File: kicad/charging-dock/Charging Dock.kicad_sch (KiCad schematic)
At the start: 0 parts

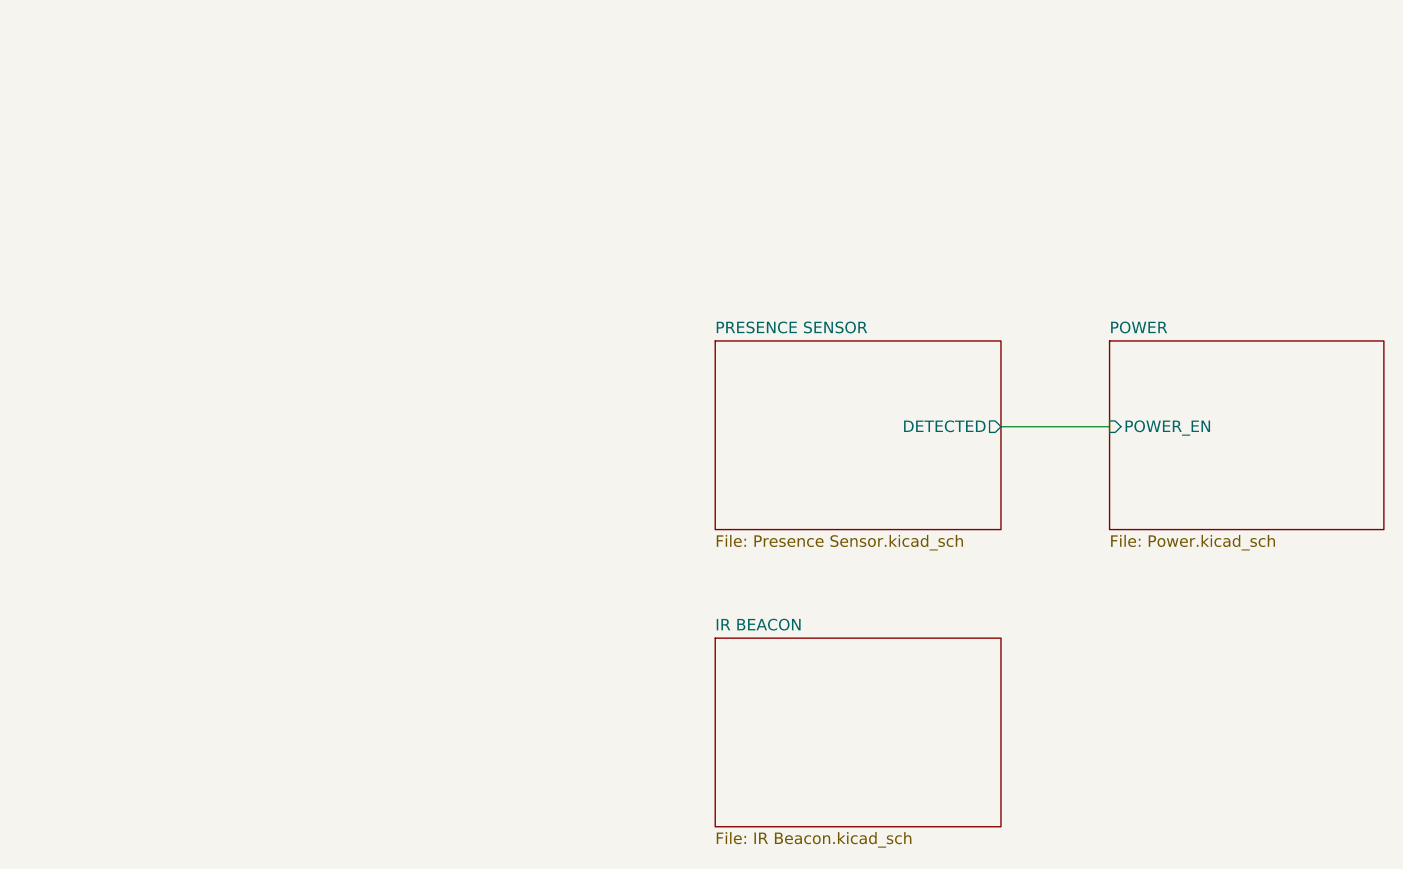
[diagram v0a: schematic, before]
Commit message: Charging dock rev 2; main-phone bucks AP64501 -> TPS54560B
Charging dock (kicad/charging-dock), redesigned:
- CH32V003F4P6 control (Arduino core, ch32fun, PlatformIO)
- robot detection: resistance-signature probe before DOCK+ goes live
- AO4407C soft-start output switch, 50 mOhm + INA180A1 current sense
- NEC IR beacon: two 3x TSAL6200 strings, AC-coupled gates
- 20 V input: DC-044A-20A, 5 A fuse, SMAJ22A, HT7533-1
- refs 8xxx for the one-panel plan; uses the shared ../main libraries
- removed the orphan sheets, the old local library copy and an unrelated PDF
- README with pin map, detection math, firmware rules, layout notes

main-phone: U21/U22 TPS54560B (AP64501 out of stock) with SS56 catch
diodes, 232k RT, 4.7k + 47nF compensation, U21 EN divider; BAT-VCC input
caps 10uF/50V 1206. SPEC and READMEs updated.

Co-Authored-By: Claude Opus 5.5 (1M context) <noreply@anthropic.com>
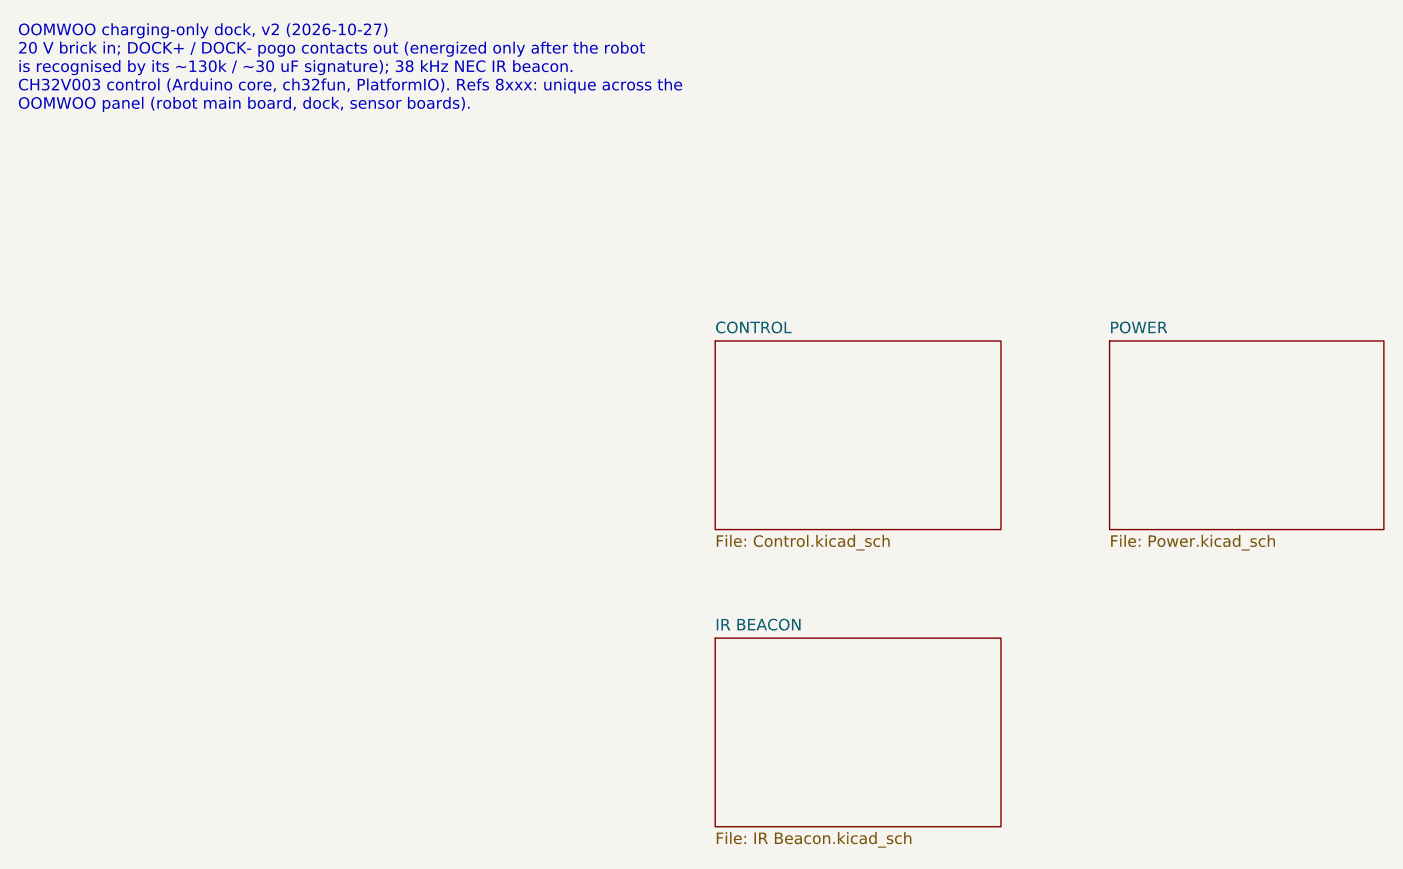
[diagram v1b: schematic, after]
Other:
- sheet PRESENCE SENSOR renamed CONTROL
- sheet CONTROL: file Presence Sensor.kicad_sch -> Control.kicad_sch
- sheet CONTROL ports: added none; removed DETECTED
- sheet POWER ports: added none; removed POWER_EN
- note added: "OOMWOO charging-only dock, v2 (2026-10-27) 20 V brick in; DOCK+ / DOCK- pogo contacts out (energized only after the robot is recognised by its ~130k / ~30 uF signature); 38 kHz NEC IR beacon. CH32V003 control (Arduino core, ch32fun, PlatformIO). Refs 8xxx: unique across the OOMWOO panel (robot main board, dock, sensor boards)."
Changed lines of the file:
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@@
 	(generator_version "10.0")
 	(paper "A4")
-	(wire
-		(pts
-			(xy 149.86 75.565) (xy 161.925 75.565)
-		)
-		(stroke
-			(width 0)
-			(type default)
-		)
-	)
 	(sheet
 		(at 118.11 99.06)
@@
 			)
 		)
-		(pin "POWER_EN" input
-			(at 161.925 75.565 180)
-			(effects
-				(font
-					(size 1.27 1.27)
-				)
-				(justify left)
-			)
-		)
 		(instances
 			(project "Charging Dock"
@@
 			(color 0 0 0 0)
 		)
-		(property "Sheetname" "PRESENCE SENSOR"
+		(property "Sheetname" "CONTROL"
 			(at 118.11 65.3284 0)
 			(show_name no)
@@
 			)
 		)
-		(property "Sheetfile" "Presence Sensor.kicad_sch"
+		(property "Sheetfile" "Control.kicad_sch"
 			(at 118.11 87.5796 0)
 			(show_name no)
@@
 			)
 		)
-		(pin "DETECTED" output
-			(at 149.86 75.565 0)
-			(effects
-				(font
-					(size 1.27 1.27)
-				)
-				(justify right)
-			)
-		)
 		(instances
 			(project "Charging Dock"
@@
 		)
 	)
+	(text "OOMWOO charging-only dock, v2 (2026-10-27)\n20 V brick in; DOCK+ / DOCK- pogo contacts out (energized only after the robot\nis recognised by its ~130k / ~30 uF signature); 38 kHz NEC IR beacon.\nCH32V003 control (Arduino core, ch32fun, PlatformIO). Refs 8xxx: unique across the\nOOMWOO panel (robot main board, dock, sensor boards)."
+		(exclude_from_sim no)
+		(at 40.64 40.64 0)
+		(effects
+			(font
+				(size 1.27 1.27)
+			)
+			(justify left bottom)
+		)
+	)

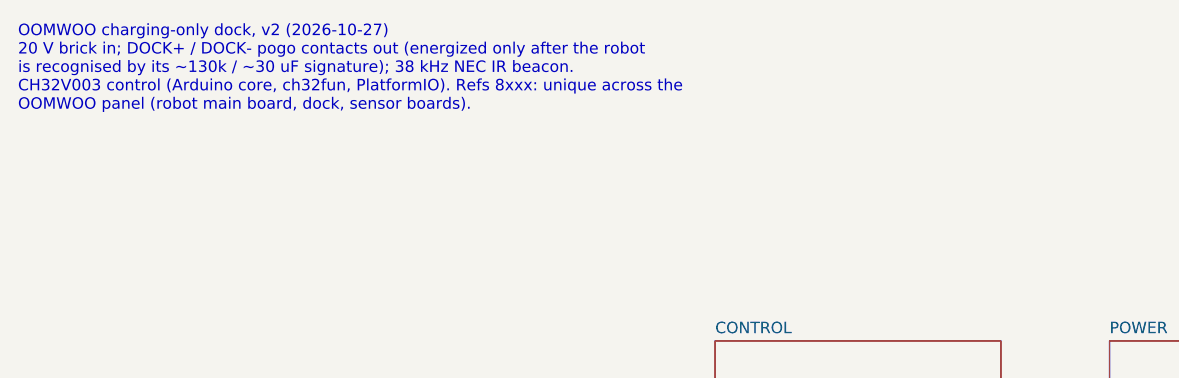
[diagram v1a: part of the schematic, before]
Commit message: Per-board reference ranges, J1 spare header, IMU AD0 pull-down, BOM outputs
- reference ranges: main-phone 1-999, dock 1000s, front ToF 2000s, side 3000s,
  cliff 4000s, rear IR 5000s, Hall 6000s (main-phone 7xxx parts renumbered
  below 1000; sensor boards and dock moved from 8xxx)
- main-phone: J7301 -> J1, a fitted 2x7 0.1" header with spares only
  (3.3 V, 5 V, I2C4, UART PC10/PC11, PA8-PA10, PD4, PE2, PE6, GND)
- IMU: AP_AD0 pulled low by R217 (address 0x68); INT2 on test pad TP1;
  FSYNC reachable on R211; R18/R72 removed
- tools/export.py replaces export_pdfs.py: schematic PDF and JLC-style BOM in
  each board's output/ folder; --pcb adds Gerbers, placement and STEP
- cliff and rear IR projects: fix top-level sheet left over from a copy
- Hall board: visual tidy-up

Co-Authored-By: Claude Opus 5.5 <noreply@anthropic.com>
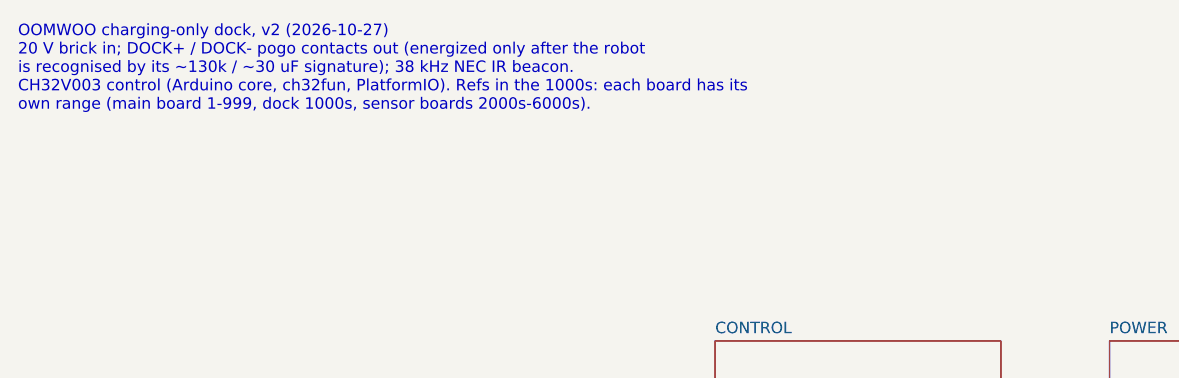
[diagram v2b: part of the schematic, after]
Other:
- note added: "OOMWOO charging-only dock, v2 (2026-10-27) 20 V brick in; DOCK+ / DOCK- pogo contacts out (energized only after the robot is recognised by its ~130k / ~30 uF signature); 38 kHz NEC IR beacon. CH32V003 control (Arduino core, ch32fun, PlatformIO). Refs in the 1000s: each board has its own range (main board 1-999, dock 1000s, sensor boards 2000s-6000s)."
- note removed: "OOMWOO charging-only dock, v2 (2026-10-27) 20 V brick in; DOCK+ / DOCK- pogo contacts out (energized only after the robot is recognised by its ~130k / ~30 uF signature); 38 kHz NEC IR beacon. CH32V003 control (Arduino core, ch32fun, PlatformIO). Refs 8xxx: unique across the OOMWOO panel (robot main board, dock, sensor boards)."
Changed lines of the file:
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@@
 		)
 	)
-	(text "OOMWOO charging-only dock, v2 (2026-10-27)\n20 V brick in; DOCK+ / DOCK- pogo contacts out (energized only after the robot\nis recognised by its ~130k / ~30 uF signature); 38 kHz NEC IR beacon.\nCH32V003 control (Arduino core, ch32fun, PlatformIO). Refs 8xxx: unique across the\nOOMWOO panel (robot main board, dock, sensor boards)."
+	(text "OOMWOO charging-only dock, v2 (2026-10-27)\n20 V brick in; DOCK+ / DOCK- pogo contacts out (energized only after the robot\nis recognised by its ~130k / ~30 uF signature); 38 kHz NEC IR beacon.\nCH32V003 control (Arduino core, ch32fun, PlatformIO). Refs in the 1000s: each board has its\nown range (main board 1-999, dock 1000s, sensor boards 2000s-6000s)."
 		(exclude_from_sim no)
 		(at 40.64 40.64 0)
